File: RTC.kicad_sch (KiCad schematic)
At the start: 14 parts, among them J17 Molex 470531000, U11 EMC2301-1-ACZL-TR, U14 74LVC1G07SE-7, U8 PCF85063AT/AAZ, Y2 X32K768S301

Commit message: removed HDMI, CAM and DISP1 connectors
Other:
- company: © 2020-2022 Raspberry Pi Ltd (formerly Raspberry Pi (Trading) Ltd.) -> (none)
- title: Compute Module 4 IO Board - RTC - FAN -> Bitcart
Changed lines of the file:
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@@
   (paper "A4")
   (title_block
-    (title "Compute Module 4 IO Board - RTC - FAN")
+    (title "Bitcart")
+    (date "2023-09-15")
     (rev "1")
-    (company "© 2020-2022 Raspberry Pi Ltd (formerly Raspberry Pi (Trading) Ltd.)")
-    (comment 1 "www.raspberrypi.com")
   )
   (junction (at 144.78 140.97) (diameter 1.016) (color 0 0 0 0)

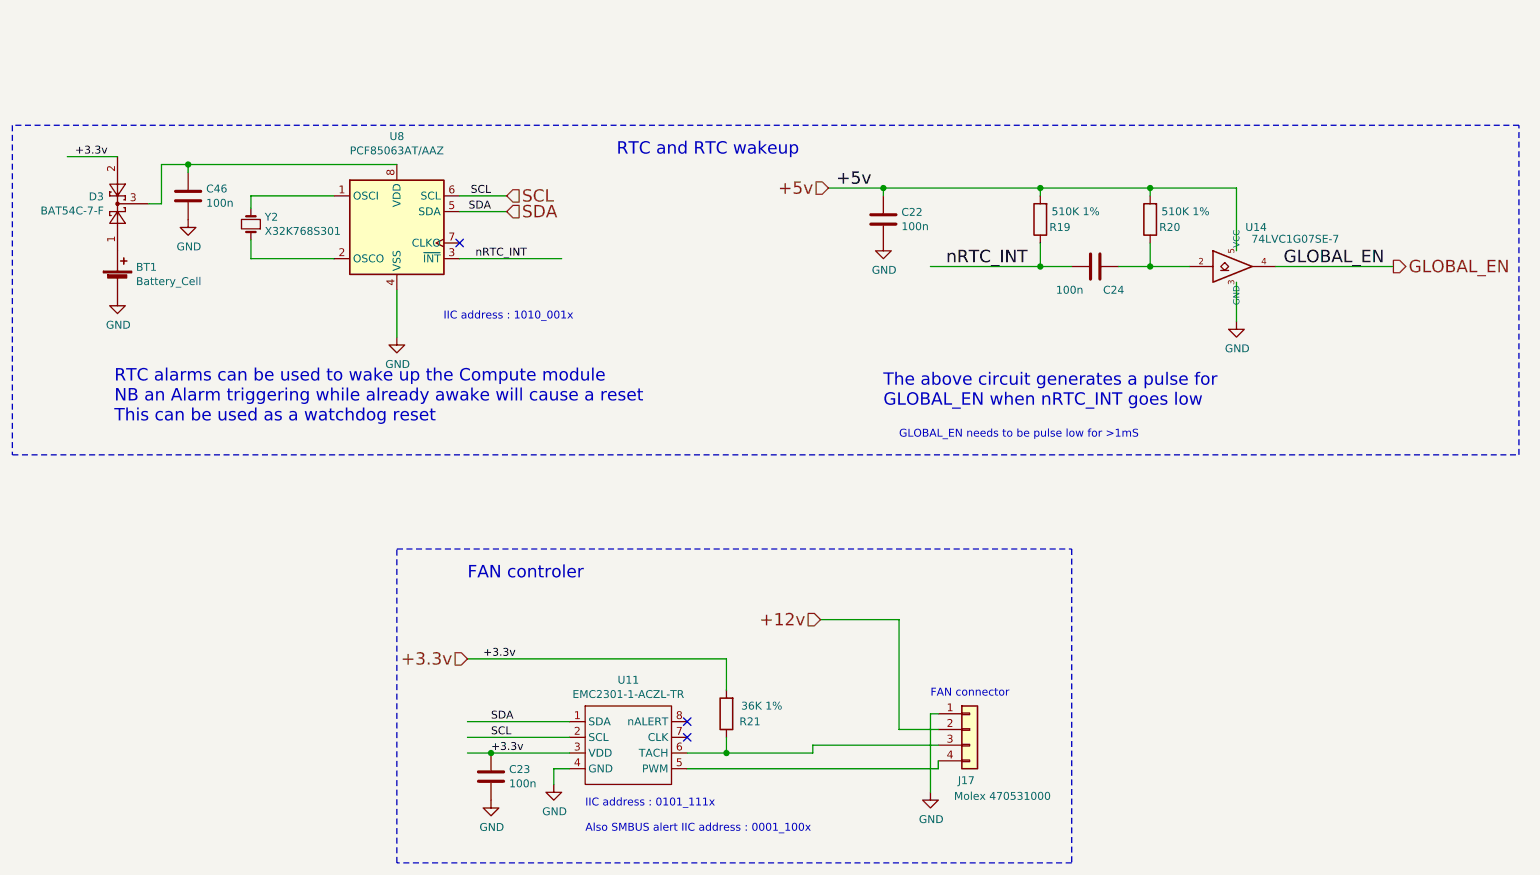
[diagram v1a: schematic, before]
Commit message: extended the board to make room for IO connectors. added the vertical display connector.
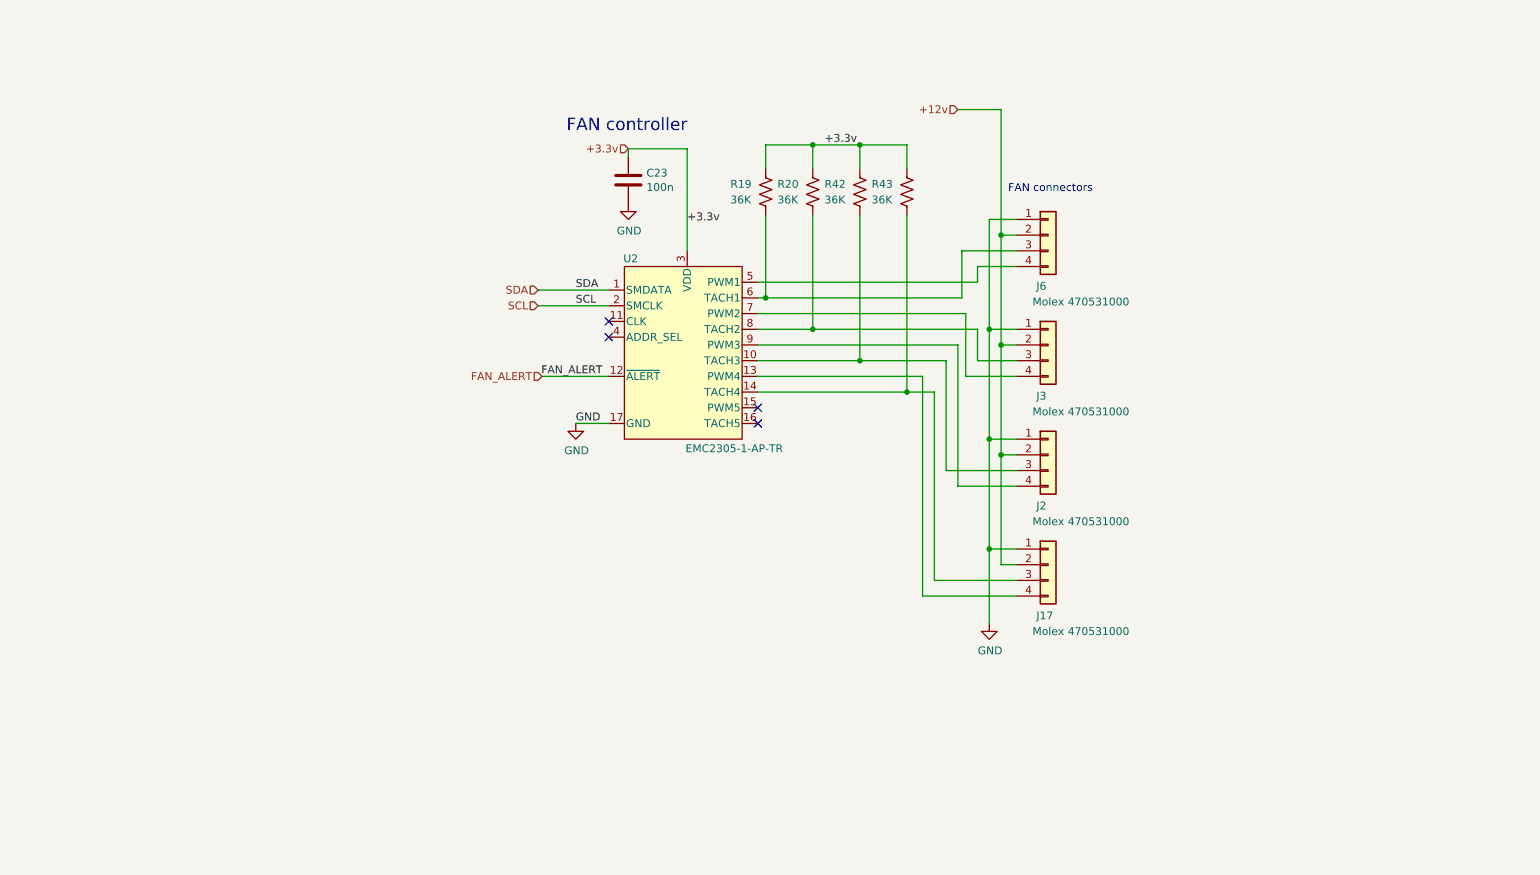
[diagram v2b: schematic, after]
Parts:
- removed BT1: Battery_Cell, Battery:BatteryHolder_Keystone_3034_1x20mm, symbol Device:Battery_Cell
- removed C22, C24, C46: 100n, Capacitor_SMD:C_0402_1005Metric, symbol Device:C
- removed D3: BAT54C-7-F, Package_TO_SOT_SMD:SOT-23, symbol Diode:BAT54C
- removed R19, R20: 510K 1%, Resistor_SMD:R_0402_1005Metric, symbol Device:R
- removed R21: 36K 1%, Resistor_SMD:R_0402_1005Metric, symbol Device:R
- removed U11: EMC2301-1-ACZL-TR, Package_SO:MSOP-8_3x3mm_P0.65mm, symbol CM4IO:EMC2301
- removed U14: 74LVC1G07SE-7, Package_TO_SOT_SMD:SOT-353_SC-70-5, symbol CM4IO:74LVC1G07_copy
- removed U8: PCF85063AT/AAZ, Package_SO:SOIC-8_3.9x4.9mm_P1.27mm, symbol Timer_RTC:PCF8563T
- removed Y2: X32K768S301, Crystal:Crystal_SMD_3215-2Pin_3.2x1.5mm, symbol Device:Crystal_Small
- added J2, J3, J6: Molex 470531000, Connector:FanPinHeader_1x04_P2.54mm_Vertical, symbol Connector_Generic:Conn_01x04
- added R19, R20, R42, R43: 36K, Resistor_SMD:R_0402_1005Metric, symbol Device:R_US
- added U2: EMC2305-1-AP-TR, bitcart:QFN16_4x4MC_MCH, symbol bitcart:EMC2305-1-AP-TR
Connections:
- net +12v: now also J2.2 (Pin_2), J3.2 (Pin_2), J6.2 (Pin_2)
- net +3.3v: now also R19.1, R20.1, R42.1, R43.1, U2.3 (VDD)
- net GND: now also J2.1 (Pin_1), J3.1 (Pin_1), J6.1 (Pin_1), U2.17 (GND)
- net SCL: now also U2.2 (SMCLK)
- net SDA: now also U2.1 (SMDATA)
- net at J17.4 (Pin_4): now also U2.13 (PWM4)
- net at J17.3 (Pin_3): now also R43.2, U2.14 (TACH4)
- new net: J2.3 (Pin_3), R42.2, U2.10 (TACH3)
- new net: J6.4 (Pin_4), U2.5 (PWM1)
- new net: J6.3 (Pin_3), R19.2, U2.6 (TACH1)
- new net: J3.4 (Pin_4), U2.7 (PWM2)
- new net: J3.3 (Pin_3), R20.2, U2.8 (TACH2)
- new net: J2.4 (Pin_4), U2.9 (PWM3)
- new net FAN_ALERT: U2.12 (~{ALERT})
- no-connect marks 3 -> 4
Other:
- note added: "FAN connectors"
- note added: "FAN controller"
- note removed: "Also SMBUS alert IIC address : 0001_100x"
- note removed: "FAN connector"
- note removed: "FAN controler"
- note removed: "GLOBAL_EN needs to be pulse low for >1mS"
- note removed: "IIC address : 0101_111x"
- note removed: "IIC address : 1010_001x"
- note removed: "RTC alarms can be used to wake up the Compute module NB an Alarm triggering while already awake will cause a reset This can be used as a watchdog reset"
- note removed: "RTC and RTC wakeup"
- note removed: "The above circuit generates a pulse for GLOBAL_EN when nRTC_INT goes low"
- moved on the sheet: C23, J17

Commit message: added a lot more parts
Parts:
- C23: value 100n -> 0.1uF; DK (none) -> 478-KGM05AR71C104KHCT-ND; Field4 Farnell -> (none); Field5 2611911 -> (none); Field6 RM EMK105 B7104KV-F -> (none); Field7 TAIYO YUDEN EUROPE GMBH -> (none); Field8 110091611 -> (none); PARTNO (none) -> KGM05AR71C104KH; Part Description 0.1uF 10% 16V Ceramic Capacitor X7R 0402 (1005 Metric) -> (none)
- J17, J2, J3: DK (none) -> WM4330-ND; PARTNO (none) -> 470531000; Part Description Connector Header Through Hole 4 position 0.100" (2.54mm) -> (none)
- J6: DK (none) -> WM4330-ND; Field4 Farnell -> (none); Field5 2313705 -> (none); Field7 Molex -> (none); PARTNO (none) -> 470531000; Part Description Connector Header Through Hole 4 position 0.100" (2.54mm) -> (none)
- R19, R20, R42, R43: DK (none) -> CR0402-FX-3602GLFCT-ND; PARTNO (none) -> CR0402-FX-3602GLF
- U2: DK (none) -> EMC2305-1-AP-CT-ND; PARYNO (none) -> EMC2305-1-AP-TR
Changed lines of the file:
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@@
   (junction (at 187.325 107.95) (diameter 0) (color 0 0 0 0)
+  )
+  (junction (at 128.905 43.18) (diameter 0) (color 0 0 0 0)
   )
   (junction (at 173.99 82.55) (diameter 0) (color 0 0 0 0)
@@
     (stroke (width 0) (type default))
   )
+  (wire (pts (xy 122.555 43.18) (xy 128.905 43.18))
+    (stroke (width 0) (type default))
+  )
   (wire (pts (xy 151.13 42.545) (xy 151.13 46.355))
     (stroke (width 0) (type default))
@@
     (effects (font (size 1.27 1.27)) (justify left bottom))
   )
-  (hierarchical_label "+3.3v" (shape input) (at 128.905 43.18 180) (fields_autoplaced)
+  (hierarchical_label "+3.3v" (shape input) (at 122.555 43.18 180) (fields_autoplaced)
     (effects (font (size 1.27 1.27)) (justify right))
   )
@@
       (effects (font (size 1.27 1.27)) (justify left))
     )
-    (property "Value" "100n" (at 131.826 49.403 0)
+    (property "Value" "0.1uF" (at 131.826 49.403 0)
       (effects (font (size 1.27 1.27)) (justify left))
     )
@@
       (effects (font (size 1.27 1.27)) hide)
     )
-    (property "Field4" "Farnell" (at 128.905 48.26 0)
-      (effects (font (size 1.27 1.27)) hide)
-    )
-    (property "Field5" "2611911" (at 128.905 48.26 0)
-      (effects (font (size 1.27 1.27)) hide)
-    )
-    (property "Field6" "RM EMK105 B7104KV-F" (at 128.905 48.26 0)
-      (effects (font (size 1.27 1.27)) hide)
-    )
-    (property "Field7" "TAIYO YUDEN EUROPE GMBH" (at 128.905 48.26 0)
-      (effects (font (size 1.27 1.27)) hide)
-    )
-    (property "Part Description" "	0.1uF 10% 16V Ceramic Capacitor X7R 0402 (1005 Metric)" (at 128.905 48.26 0)
-      (effects (font (size 1.27 1.27)) hide)
-    )
-    (property "Field8" "110091611" (at 128.905 48.26 0)
+    (property "DK" "478-KGM05AR71C104KHCT-ND" (at 128.905 48.26 0)
+      (effects (font (size 1.27 1.27)) hide)
+    )
+    (property "PARTNO" "KGM05AR71C104KH" (at 128.905 48.26 0)
       (effects (font (size 1.27 1.27)) hide)
     )
@@
       (effects (font (size 1.27 1.27)) hide)
     )
-    (property "Part Description" "	Connector Header Through Hole 4 position 0.100\" (2.54mm)" (at 196.85 110.49 0)
+    (property "Part Description" "" (at 196.85 110.49 0)
+      (effects (font (size 1.27 1.27)) hide)
+    )
+    (property "DK" "WM4330-ND" (at 196.85 110.49 0)
+      (effects (font (size 1.27 1.27)) hide)
+    )
+    (property "PARTNO" "470531000" (at 196.85 110.49 0)
       (effects (font (size 1.27 1.27)) hide)
     )
@@
       (effects (font (size 1.27 1.27) italic) hide)
     )
-    (property "Datasheet" "EMC2305-1-AP-TR" (at 187.96 62.23 0)
+    (property "Datasheet" "https://ww1.microchip.com/downloads/aemDocuments/documents/MSLD/ProductDocuments/DataSheets/EMC2301-2-3-5-Data-Sheet-DS20006532A.pdf" (at 187.96 62.23 0)
       (effects (font (size 1.27 1.27) italic) hide)
+    )
+    (property "DK" "EMC2305-1-AP-CT-ND" (at 137.16 74.93 0)
+      (effects (font (size 1.27 1.27)) hide)
+    )
+    (property "PARYNO" "EMC2305-1-AP-TR" (at 137.16 74.93 0)
+      (effects (font (size 1.27 1.27)) hide)
     )
     (pin "1")
@@
       (effects (font (size 1.27 1.27)) hide)
     )
+    (property "DK" "CR0402-FX-3602GLFCT-ND" (at 151.13 50.165 0)
+      (effects (font (size 1.27 1.27)) hide)
+    )
+    (property "PARTNO" "CR0402-FX-3602GLF" (at 151.13 50.165 0)
+      (effects (font (size 1.27 1.27)) hide)
+    )
     (pin "1")
     (pin "2")
@@
       (effects (font (size 1.27 1.27)) hide)
     )
-    (property "Field4" "Farnell" (at 196.85 57.15 0)
-      (effects (font (size 1.27 1.27)) hide)
-    )
-    (property "Field5" "	2313705" (at 196.85 57.15 0)
+    (property "DK" "WM4330-ND" (at 196.85 57.15 0)
       (effects (font (size 1.27 1.27)) hide)
     )
@@
       (effects (font (size 1.27 1.27)) hide)
     )
-    (property "Field7" "Molex" (at 196.85 57.15 0)
-      (effects (font (size 1.27 1.27)) hide)
-    )
-    (property "Part Description" "	Connector Header Through Hole 4 position 0.100\" (2.54mm)" (at 196.85 57.15 0)
+    (property "PARTNO" "470531000" (at 196.85 57.15 0)
       (effects (font (size 1.27 1.27)) hide)
     )
@@
       (effects (font (size 1.27 1.27)) hide)
     )
+    (property "DK" "CR0402-FX-3602GLFCT-ND" (at 166.37 50.165 0)
+      (effects (font (size 1.27 1.27)) hide)
+    )
+    (property "PARTNO" "CR0402-FX-3602GLF" (at 166.37 50.165 0)
+      (effects (font (size 1.27 1.27)) hide)
+    )
     (pin "1")
     (pin "2")
@@
       (effects (font (size 1.27 1.27)) hide)
     )
+    (property "DK" "CR0402-FX-3602GLFCT-ND" (at 158.75 50.165 0)
+      (effects (font (size 1.27 1.27)) hide)
+    )
+    (property "PARTNO" "CR0402-FX-3602GLF" (at 158.75 50.165 0)
+      (effects (font (size 1.27 1.27)) hide)
+    )
     (pin "1")
     (pin "2")
@@
       (effects (font (size 1.27 1.27)) hide)
     )
+    (property "DK" "CR0402-FX-3602GLFCT-ND" (at 173.99 50.165 0)
+      (effects (font (size 1.27 1.27)) hide)
+    )
+    (property "PARTNO" "CR0402-FX-3602GLF" (at 173.99 50.165 0)
+      (effects (font (size 1.27 1.27)) hide)
+    )
     (pin "1")
     (pin "2")
@@
       (effects (font (size 1.27 1.27)) hide)
     )
-    (property "Part Description" "	Connector Header Through Hole 4 position 0.100\" (2.54mm)" (at 196.85 92.71 0)
+    (property "Part Description" "" (at 196.85 92.71 0)
+      (effects (font (size 1.27 1.27)) hide)
+    )
+    (property "DK" "WM4330-ND" (at 196.85 92.71 0)
+      (effects (font (size 1.27 1.27)) hide)
+    )
+    (property "PARTNO" "470531000" (at 196.85 92.71 0)
       (effects (font (size 1.27 1.27)) hide)
     )
@@
       (effects (font (size 1.27 1.27)) hide)
     )
-    (property "Part Description" "	Connector Header Through Hole 4 position 0.100\" (2.54mm)" (at 196.85 74.93 0)
-      (effects (font (size 1.27 1.27)) hide)
-    )
+    (property "Part Description" "" (at 196.85 74.93 0)
+      (effects (font (size 1.27 1.27)) hide)
+    )
+    (property "DK" "WM4330-ND" (at 196.85 74.93 0)
+      (effects (font (size 1.27 1.27)) hide)
+    )
+    (property "PARTNO" "470531000" (at 196.85 74.93 0)
+      (effects (font (size 1.27 1.27)) hide)
+    )
